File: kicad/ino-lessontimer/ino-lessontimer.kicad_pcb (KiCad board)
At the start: 2 copper layers, 83.8 x 55.9 mm, 10 parts, among them SW1 BTNMinus, SW2 BTNPlus, SW3 BTNSet, SW4 BTNShow

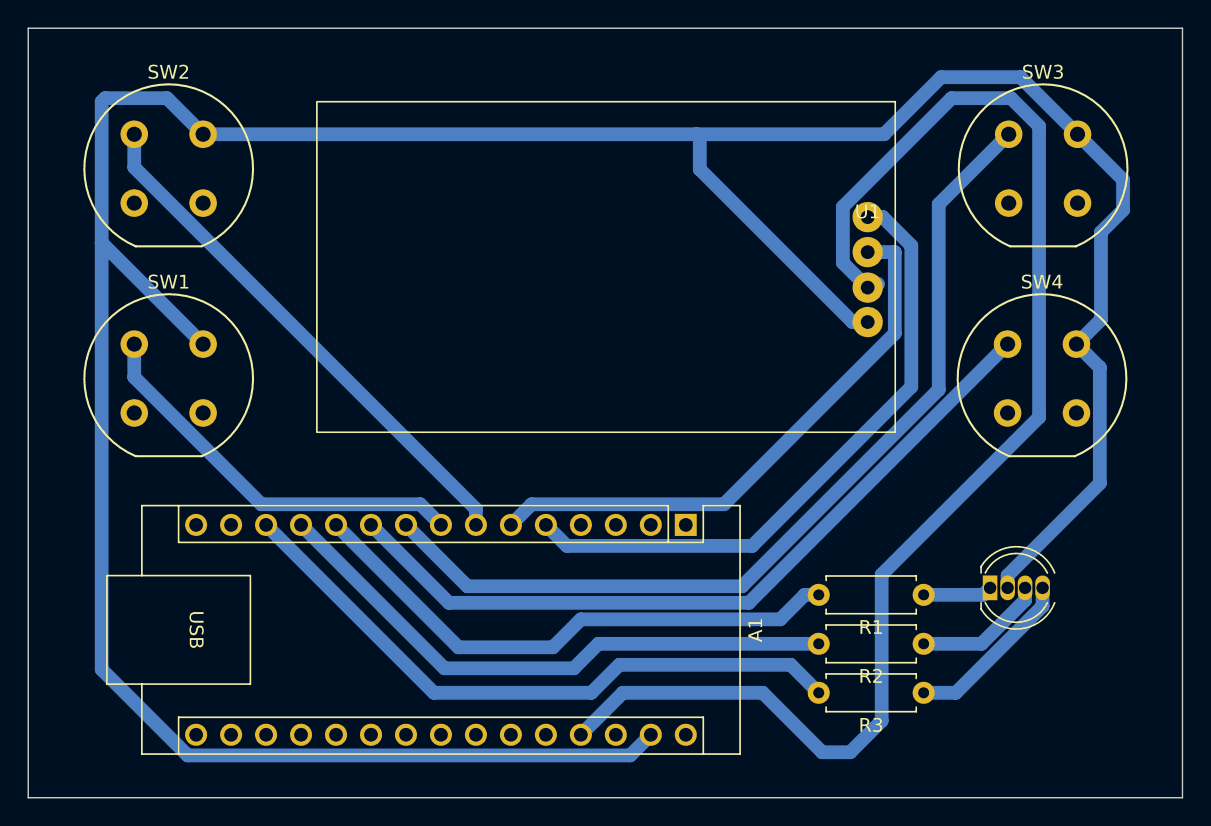
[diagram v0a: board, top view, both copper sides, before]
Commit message: Fixed PCB track spacing
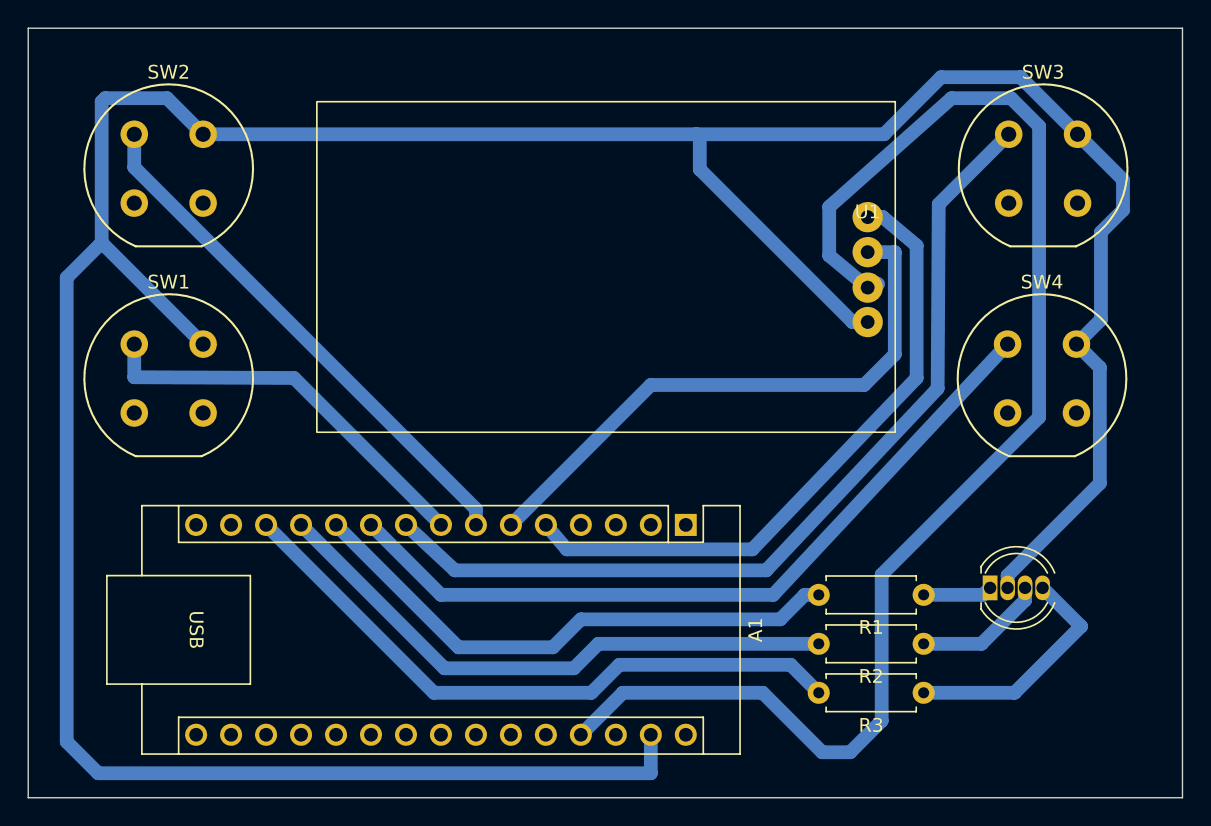
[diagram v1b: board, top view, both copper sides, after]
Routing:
- net GND: track 228.8 -> 238.2 mm
- net Net-(D1-BA): track 12.6 -> 17.4 mm
- net +5V: track 98.8 -> 100.1 mm
- net Net-(A1-D6): track 67.1 -> 66.2 mm
- net Net-(A1-D3): track 41.5 -> 42.4 mm
- net Net-(A1-D2): track 46.2 -> 47.0 mm
